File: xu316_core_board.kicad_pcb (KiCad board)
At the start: 2 copper layers, 60.5 x 67.8 mm, 91 parts, among them CN1 HX JN1.27-2x10P ZZ H4.9, J1 Conn_01x08, J10 Conn_02x04_Odd_Even, J11 Conn_02x05_Odd_Even, J12 Conn_02x04_Odd_Even, J13 Conn_02x05_Odd_Even, J2 Conn_01x06, J3 Conn_01x10, J4 Conn_01x08, J5 Conn_02x05_Odd_Even, J6 Conn_02x02_Odd_Even, J7 Conn_02x04_Odd_Even, J8 Conn_01x02, J9 Conn_02x05_Odd_Even, Q1 SI1024X, SW1 RESET, U1 XU316-1024-QF60A-C32, U2 W25Q64JWUUIQ, U3 TPS62A0569PDRLR, U4 TPS62402DRCR, U5 LMR51450, U7 NUP4114, Y2 24MHz

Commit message: start routing
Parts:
- removed J5: Conn_02x05_Odd_Even, Connector_PinHeader_2.54mm:PinHeader_2x05_P2.54mm_Vertical
- added D1: D_Schottky_Small, Diode_SMD:D_SMA, F.Cu at (187.1, 102.1)
- added D2: D_Schottky_Small, Diode_SMD:D_SMA, F.Cu at (187.1, 106.6)
- added F1: 5A, Fuse:Fuse_2512_6332Metric, F.Cu at (138.2, 60.5)
- added FB1: 120R 2A, Inductor_SMD:L_0603_1608Metric, F.Cu at (178.7, 117.8)
- added J15: Jack-DC, Connector_BarrelJack:BarrelJack_CUI_PJ-063AH_Horizontal, F.Cu at (138.1, 54.6)
- added J16: Conn_02x06_Odd_Even, Connector_PinHeader_2.54mm:PinHeader_2x06_P2.54mm_Vertical, F.Cu at (107.0, 80.2)
- added R22: 0.1, Resistor_SMD:R_0402_1005Metric, F.Cu at (184.5, 109.9)
- added R23: 0.1, Resistor_SMD:R_0402_1005Metric, F.Cu at (184.5, 111.9)
- L1: footprint Inductor_SMD:L_0402_1005Metric -> Inductor_SMD:L_1008_2520Metric
- moved C21 92.2 mm to (130.0, 78.0)
- moved U3 90.3 mm to (129.5, 79.6), turned to -90 degrees
- moved C23 82.7 mm to (133.5, 81.7), turned to -90 degrees
- moved L1 82.1 mm to (132.6, 78.8), turned to -90 degrees
- moved R6 81.6 mm to (133.5, 83.6), turned to -90 degrees
- moved R5 80.8 mm to (132.5, 81.7), turned to 90 degrees
- moved Y2 79.2 mm to (120.9, 90.5)
- moved C22 79.1 mm to (130.4, 81.8), turned to 90 degrees
- moved R4 78.7 mm to (131.4, 81.7), turned to -90 degrees
- moved C3 76.9 mm to (122.9, 90.2), turned to -90 degrees
- moved C2 72.2 mm to (118.9, 90.8), turned to -90 degrees
- moved J11 68.6 mm to (109.9, 59.4), turned to 90 degrees
- moved R3 64.8 mm to (120.5, 88.7), turned to 180 degrees
- moved R2 62.1 mm to (118.9, 88.9), turned to -90 degrees
- moved L3 61.9 mm to (133.4, 91.2)
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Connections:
- C21 pad 1: +5V -> +5V(CORE)
- C24 pad 1: +5V -> +5V(IO)
- R7 pad 1: +5V -> +5V(IO)
- R8 pad 1: +5V -> +5V(IO)
- U2 pad 2: /X0P16A2 -> /X0P16A3
- U3 pad 3: +5V -> +5V(CORE)
- U3 pad 5: +5V -> +5V(CORE)
- U4 pad 3: +5V -> +5V(IO)
- U4 pad 5: +5V -> +5V(IO)
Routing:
- net +0.9V: track 0.00 -> 16.6 mm, vias 0 -> 4
- net /X0P1B0: track 0.00 -> 8.60 mm
- net /X0P16A3: track 0.00 -> 7.11 mm
- net /X0P16A4: track 0.00 -> 5.80 mm
- net /XU316 Core/XOUT: track 0.00 -> 3.78 mm
- net /X0P16A2: track 0.00 -> 3.31 mm
- net /XU316 Core/XIN: track 0.00 -> 2.58 mm
- net Net-(C2-Pad1): track 0.00 -> 2.57 mm
- net GND: vias 0 -> 16
- added copper zone on B.Cu, net GND
- added copper zone on F.Cu, net GND
- added copper zone on In1.Cu, net GND
- added copper zone on In2.Cu, net GND
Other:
- board size 60.5 x 67.8 mm -> 53.3 x 68.6 mm
- copper layers 2 -> 4

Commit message: sync
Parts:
- moved CN1 12.3 mm to (124.5, 99.0)
- moved C12 12.0 mm to (130.9, 88.5), turned to 0 degrees
- moved R10 11.0 mm to (136.8, 90.7)
- moved C26 7.75 mm to (133.5, 86.5), turned to 180 degrees
- moved C1 7.35 mm to (118.0, 83.7), turned to -90 degrees
- moved C22 4.76 mm to (127.9, 77.7), turned to -90 degrees
- moved C25 4.05 mm to (131.4, 94.2), turned to 90 degrees
- moved R7 3.70 mm to (129.9, 94.7), turned to 0 degrees
- moved L2 3.62 mm to (133.3, 93.2), turned to -90 degrees
- moved R6 3.60 mm to (130.4, 81.7)
- moved U3 3.05 mm to (132.6, 79.6), turned to 90 degrees
- moved R9 2.94 mm to (137.9, 90.7)
- moved C21 2.87 mm to (132.8, 78.0), turned to 180 degrees
- moved L1 2.76 mm to (129.8, 78.7), turned to 90 degrees
- moved R8 2.71 mm to (129.9, 93.6), turned to 0 degrees
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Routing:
- net +0.9V: track 16.6 -> 25.8 mm, vias 4 -> 6
- net /X0P16A5: track 0.00 -> 9.09 mm
- net /X0P1C0: track 0.00 -> 9.06 mm
- net Net-(U4-EN2): track 0.00 -> 7.45 mm, vias 0 -> 2
- net +1.8V: track 0.00 -> 7.40 mm, vias 0 -> 2
- net +3.3V: track 0.00 -> 7.37 mm, vias 0 -> 2
- net Net-(U4-EN1): track 0.00 -> 6.51 mm, vias 0 -> 2
- net /X0P16A2: track 3.31 -> 9.05 mm
- net Net-(U3-FB): track 0.00 -> 5.08 mm
- net /X0P16A4: track 5.80 -> 9.02 mm
- net /X0P16A3: track 7.11 -> 8.99 mm
- net +5V(CORE): track 0.00 -> 1.69 mm
- net +5V(IO): track 0.00 -> 1.67 mm
- added copper zone on In2.Cu, net +0.9V
- added copper zone on F.Cu, net +5V(CORE)
- added copper zone on F.Cu, net +5V(IO)
- added copper zone on F.Cu, net Net-(U3-SW)
- added copper zone on F.Cu, net Net-(U4-SW1)
- added copper zone on F.Cu, net Net-(U4-SW2)

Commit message: Routed the power rail
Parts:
- moved R10 6.81 mm to (133.1, 85.0)
- moved R9 6.79 mm to (134.2, 85.0)
- moved C12 5.97 mm to (125.1, 90.1), turned to -90 degrees
- moved C26 0.61 mm to (132.9, 86.5)
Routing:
- net +5V(IO): track 1.67 -> 4.60 mm
- net +0.9V: track 25.8 -> 28.5 mm, vias 6 -> 7
- net +1.8V: track 7.40 -> 9.83 mm, vias 2 -> 6
- net GND: track 0.00 -> 0.43 mm, vias 16 -> 17
- net +3.3V: track 7.37 -> 7.33 mm, vias 2 -> 3
- added copper zone on F.Cu, net +1.8V
- added copper zone on In2.Cu, net +1.8V
- added copper zone on F.Cu, net +3.3V
- added copper zone on In2.Cu, net +3.3V

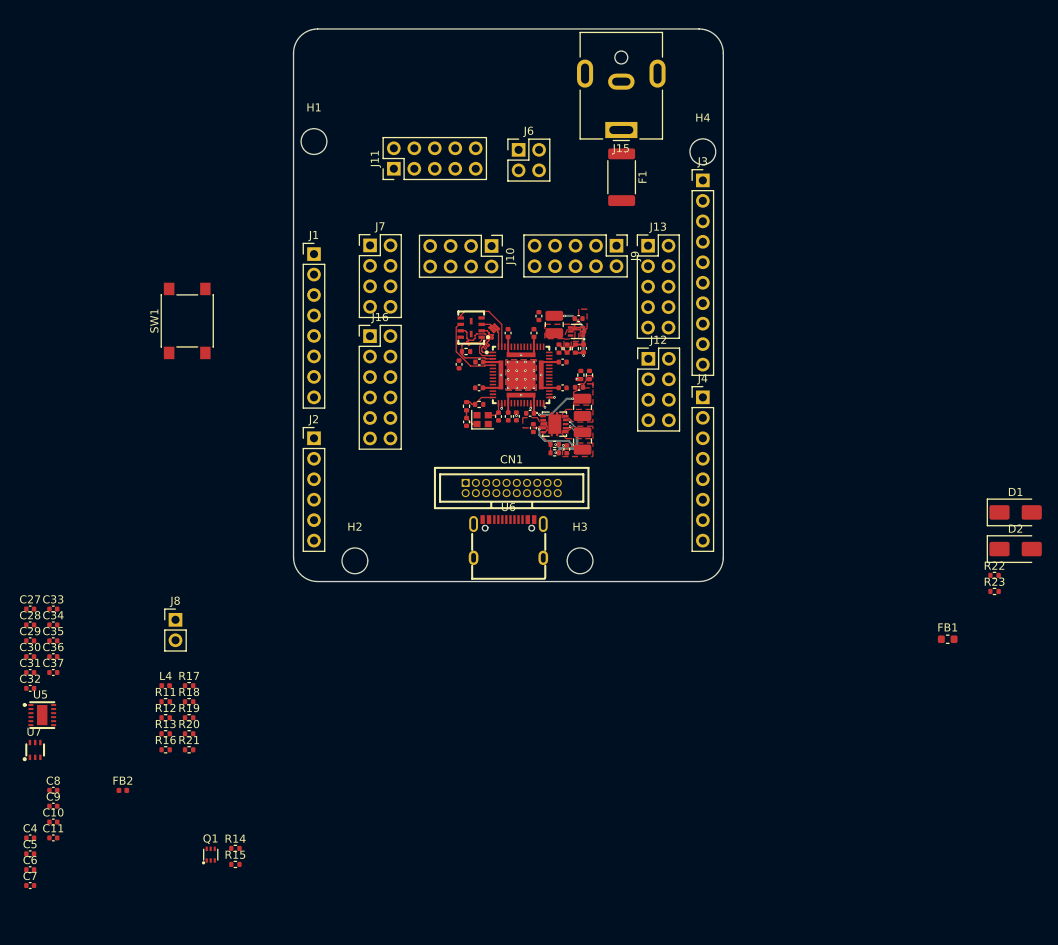
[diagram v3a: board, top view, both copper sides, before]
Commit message: Updated schem; Routed most of the IO
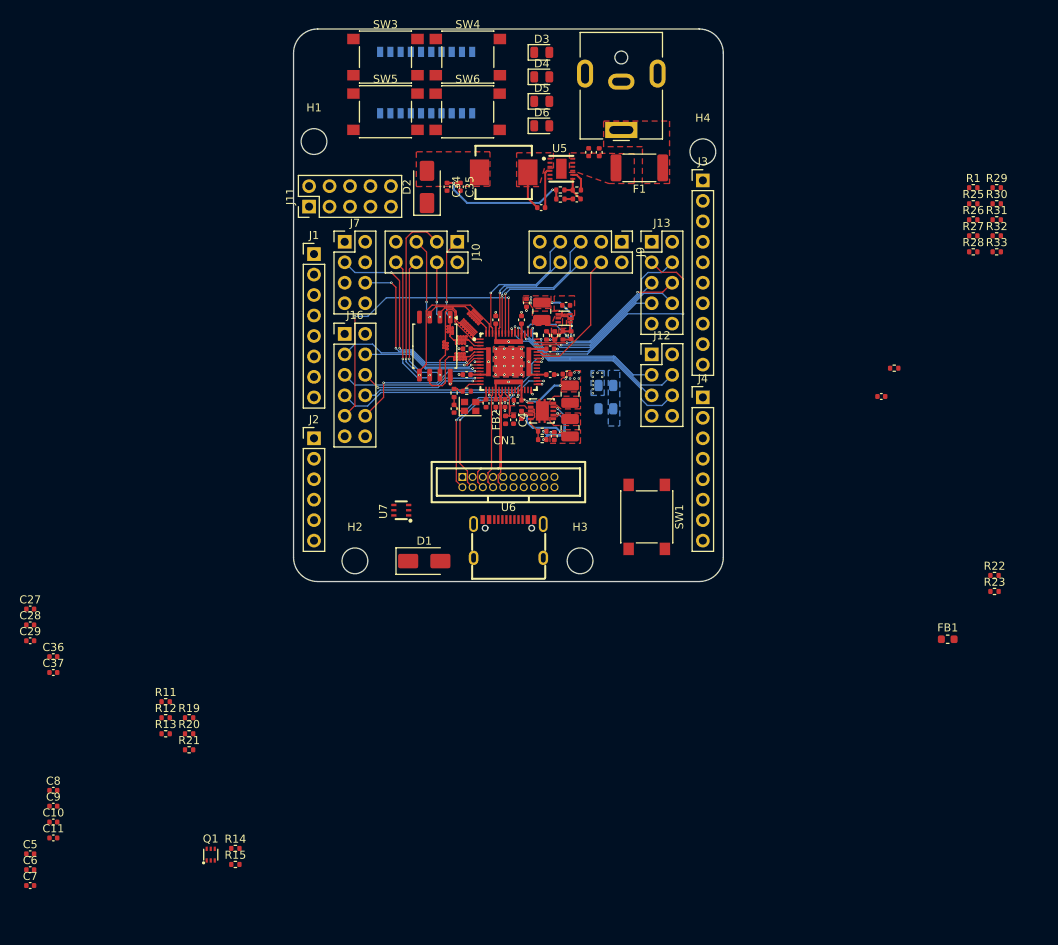
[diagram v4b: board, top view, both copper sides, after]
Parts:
- removed C1: 100N, Capacitor_SMD:C_0402_1005Metric
- removed J6: Conn_02x02_Odd_Even, Connector_PinHeader_2.54mm:PinHeader_2x02_P2.54mm_Vertical
- removed J8: Conn_01x02, Connector_PinHeader_2.54mm:PinHeader_1x02_P2.54mm_Vertical
- removed L4: 4.7uH, Inductor_SMD:L_0402_1005Metric
- removed U2: W25Q64JWUUIQ, EasyEDA_Lib:USON-8_L4.0-W3.0-P0.80-BL_WINBOND_UU
- added C38: 100N, Capacitor_SMD:C_0402_1005Metric, F.Cu at (170.4, 87.7)
- added D3: LED_GRN, LED_SMD:LED_0805_2012Metric, F.Cu at (128.3, 45.0)
- added D4: LED_GRN, LED_SMD:LED_0805_2012Metric, F.Cu at (128.3, 48.0)
- added D5: LED_GRN, LED_SMD:LED_0805_2012Metric, F.Cu at (128.3, 51.0)
- added D6: LED_GRN, LED_SMD:LED_0805_2012Metric, F.Cu at (128.3, 54.1)
- added L5: 4.7uH, EasyEDA_Lib:IND-SMD_L7.0-W6.6, F.Cu at (123.5, 59.9)
- added R24: 4.7K, Resistor_SMD:R_0402_1005Metric, F.Cu at (172.0, 84.2)
- added R25: 4.7K, Resistor_SMD:R_0402_1005Metric, F.Cu at (181.8, 63.8)
- added R26: 470, Resistor_SMD:R_0402_1005Metric, F.Cu at (181.8, 65.7)
- added R27: 470, Resistor_SMD:R_0402_1005Metric, F.Cu at (181.8, 67.7)
- added R28: 470, Resistor_SMD:R_0402_1005Metric, F.Cu at (181.8, 69.7)
- added R29: 470, Resistor_SMD:R_0402_1005Metric, F.Cu at (184.7, 61.8)
- added R30: 10K, Resistor_SMD:R_0402_1005Metric, F.Cu at (184.7, 63.8)
- added R31: 10K, Resistor_SMD:R_0402_1005Metric, F.Cu at (184.7, 65.7)
- added R32: 10K, Resistor_SMD:R_0402_1005Metric, F.Cu at (184.7, 67.7)
- added R33: 10K, Resistor_SMD:R_0402_1005Metric, F.Cu at (184.7, 69.7)
- added SW3: SW_Push, Button_Switch_SMD:SW_Push_1P1T_NO_6x6mm_H9.5mm, F.Cu at (108.9, 45.5)
- added SW4: SW_Push, Button_Switch_SMD:SW_Push_1P1T_NO_6x6mm_H9.5mm, F.Cu at (119.1, 45.5)
- added SW5: SW_Push, Button_Switch_SMD:SW_Push_1P1T_NO_6x6mm_H9.5mm, F.Cu at (108.9, 52.3)
- added SW6: SW_Push, Button_Switch_SMD:SW_Push_1P1T_NO_6x6mm_H9.5mm, F.Cu at (119.1, 52.3)
- added SW7: ~, EasyEDA_Lib:SW-SMD_20P-L14.3-W5.4-P1.27-LS8.3, B.Cu at (113.9, 48.7)
- added U8: W25Q32JVSS, Package_SO:SOIC-8_5.23x5.23mm_P1.27mm, F.Cu at (115.0, 81.4)
- C2, C3: value 100N -> 22pF
- C4: value 100N -> 1uF
- R10, R9: footprint Resistor_SMD:R_0402_1005Metric -> Resistor_SMD:R_0805_2012Metric; moved to B.Cu
- moved C31 95.7 mm to (135.4, 57.4), turned to 90 degrees
- moved U5 93.5 mm to (130.7, 59.4)
- moved C30 93.4 mm to (134.1, 57.4), turned to 90 degrees
- moved C32 87.1 mm to (128.2, 64.2), turned to 180 degrees
- moved R16 86.2 mm to (132.6, 62.0)
- moved D2 85.8 mm to (114.0, 61.7), turned to 90 degrees
- moved C33 82.5 mm to (132.6, 63.2)
- moved C4 79.3 mm to (124.8, 90.6), turned to -90 degrees
- moved R18 77.6 mm to (130.6, 63.2)
- moved R17 76.9 mm to (130.6, 62.0)
- moved C35 75.7 mm to (118.2, 61.6), turned to -90 degrees
- moved D1 73.6 mm to (113.7, 108.1)
- moved C34 73.1 mm to (116.5, 61.6), turned to -90 degrees
- moved R1 66.1 mm to (181.8, 61.8), turned to 0 degrees
- moved FB2 66.1 mm to (123.8, 90.6), turned to 90 degrees
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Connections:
- CN1 pad 13: Net-(CN1-Pad13) -> GND
- CN1 pad 15: Net-(CN1-Pad13) -> GND
- CN1 pad 17: Net-(CN1-Pad13) -> GND
- CN1 pad 19: Net-(CN1-Pad13) -> GND
- CN1 pad 3: Net-(CN1-Pad13) -> GND
- CN1 pad 5: Net-(CN1-Pad13) -> GND
- CN1 pad 7: Net-(CN1-Pad13) -> GND
- CN1 pad 9: Net-(CN1-Pad13) -> GND
- J13 pad 4: VDDIO -> /X0P16B9
- J13 pad 6: /X0P16B9 -> /X0P16B11
- J13 pad 8: /X0P16B11 -> /CORE_ADJ
- J3 pad 10: /X0P16B14 -> /X0P16B5
- J3 pad 5: /X0P16B9 -> /X0P1C0
- J3 pad 8: /X0P1D0 -> /X0P16B9
- J3 pad 9: /X0P16B5 -> /X0P16B14
- J4 pad 7: /X0P1C0 -> /X0P1D0
- J9 pad 3: /X0P16B3 -> VDDIO
- J9 pad 4: VDDIO -> /X0P16B3
- J9 pad 5: /X0P16B4 -> /X0P16B5
- J9 pad 6: /X0P16B5 -> /X0P16B4
- J9 pad 7: /X0P16B6 -> /X0P16B7
- J9 pad 8: /X0P16B7 -> /X0P16B6
- Q1 pad 1: /X0P16B11 -> /IO Headers/SDA_XMOS
- Q1 pad 2: VDDIO_I2C -> VDDIO
- Q1 pad 3: /IO Headers/I2C_SCL_PU -> /IO Headers/SCL_ARD
- Q1 pad 4: /X0P16B10 -> /IO Headers/SCL_XMOS
- Q1 pad 5: VDDIO_I2C -> VDDIO
- Q1 pad 6: /IO Headers/I2C_SDA_PU -> /IO Headers/SDA_ARD
- R1 pad 2: /X0P1B0 -> /IO Headers/SCL_XMOS
- R14 pad 2: /IO Headers/I2C_SCL_PU -> /IO Headers/SCL_ARD
- R15 pad 2: /IO Headers/I2C_SDA_PU -> /IO Headers/SDA_ARD
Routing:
- net /X1P1K0: track 0.00 -> 37.3 mm, vias 0 -> 2
- net /X0P16A2: track 9.05 -> 40.9 mm, vias 0 -> 2
- net /X0P1L0: track 0.00 -> 29.4 mm, vias 0 -> 2
- net /X1P1F0: track 0.00 -> 27.4 mm, vias 0 -> 1
- net /X0P1A0: track 0.00 -> 27.3 mm, vias 0 -> 3
- net /X0P16A5: track 9.09 -> 35.6 mm, vias 0 -> 2
- net /X0P1C0: track 9.06 -> 35.6 mm, vias 0 -> 2
- net /X0P16B15: track 0.00 -> 26.3 mm, vias 0 -> 1
- net /X1P1G0: track 0.00 -> 25.4 mm, vias 0 -> 1
- net /X0P1D0: track 0.00 -> 23.3 mm, vias 0 -> 3
- net /X0P16B13: track 0.00 -> 23.2 mm, vias 0 -> 1
- net /X0P16B11: track 0.00 -> 22.9 mm, vias 0 -> 2
- net /X0P16B9: track 0.00 -> 21.9 mm, vias 0 -> 1
- net /X0P1B0: track 9.07 -> 28.7 mm, vias 0 -> 2
- net /X0P16A4: track 9.02 -> 28.6 mm, vias 0 -> 2
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- added copper zone on F.Cu, net +0.9V
- added copper zone on B.Cu, net +3.3V
- added copper zone on F.Cu, net +Vin
- added copper zone on F.Cu, net DCDC_5V
- added copper zone on F.Cu, net Net-(C32-Pad2)
- added copper zone on F.Cu, net Net-(F1-Pad1)
- added copper zone on B.Cu, net VDDIO
- added copper zone on In2.Cu, net VDDIO

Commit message: Finish routing
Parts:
- removed R23: 0.1, Resistor_SMD:R_0402_1005Metric
- added J14: Conn_01x02, Connector_PinHeader_2.54mm:PinHeader_1x02_P2.54mm_Vertical, F.Cu at (103.9, 99.1)
- added J17: Conn_01x03, Connector_PinHeader_2.54mm:PinHeader_1x03_P2.54mm_Vertical, F.Cu at (136.4, 96.8)
- added J5: Conn_01x03, Connector_PinHeader_2.54mm:PinHeader_1x03_P2.54mm_Vertical, F.Cu at (148.3, 46.9)
- added J6: Conn_01x04, Connector_PinHeader_2.54mm:PinHeader_1x04_P2.54mm_Vertical, F.Cu at (99.4, 61.6)
- added J8: Conn_01x02, Connector_PinHeader_2.54mm:PinHeader_1x02_P2.54mm_Vertical, F.Cu at (124.2, 68.5)
- added R34: 0.1, Resistor_SMD:R_1206_3216Metric, F.Cu at (121.0, 69.7)
- J11: value Conn_02x05_Odd_Even -> Conn_01x03; footprint Connector_PinHeader_2.54mm:PinHeader_2x05_P2.54mm_Vertical -> Connector_PinHeader_2.54mm:PinHeader_1x03_P2.54mm_Vertical
- R22: footprint Resistor_SMD:R_0402_1005Metric -> Resistor_SMD:R_1206_3216Metric
- moved R15 97.0 mm to (143.5, 64.6), turned to 90 degrees
- moved R14 97.0 mm to (143.5, 62.7), turned to -90 degrees
- moved Q1 96.6 mm to (140.4, 63.9), turned to 180 degrees
- moved C6 90.9 mm to (124.7, 78.1), turned to 90 degrees
- moved C5 89.3 mm to (129.4, 82.8)
- moved C11 87.3 mm to (132.3, 83.7)
- moved R30 84.5 mm to (102.8, 43.3)
- moved C7 84.2 mm to (118.9, 83.8), turned to 180 degrees
- moved R32 83.8 mm to (102.8, 50.1)
- moved C10 81.6 mm to (129.3, 87.1)
- moved C9 81.0 mm to (129.3, 86.1)
- moved R22 79.7 mm to (105.2, 102.3)
- moved C27 73.7 mm to (137.6, 102.6), turned to -90 degrees
- moved C8 70.8 mm to (121.4, 90.5), turned to -90 degrees
- moved R13 69.7 mm to (132.3, 81.6), turned to 180 degrees
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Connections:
- J11 pad 1: +5V -> +1.8V
- J11 pad 2: +3.3V -> +1.8V
- J11 pad 3: +5V -> GND
- J3 pad 1: /IO Headers/I2C_SCL_PU -> /IO Headers/SCL_ARD
- J3 pad 2: /IO Headers/I2C_SDA_PU -> /IO Headers/SDA_ARD
- J7 pad 4: VDDIO -> /X0P1D0
- J7 pad 5: /X0P1C0 -> GND
- J7 pad 6: /X0P1D0 -> GND
- R22 pad 1: +5V(IO) -> +5V
- R22 pad 2: +5V -> +5V(IO)
- R27 pad 1: /IO Headers/LED0 -> /IO Headers/LED1
- R28 pad 1: /IO Headers/LED0 -> /IO Headers/LED2
- R29 pad 1: /IO Headers/LED0 -> /IO Headers/LED3
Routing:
- net +3.3V: track 7.33 -> 221.7 mm, vias 18 -> 16
- net +1.8V: track 9.38 -> 154.2 mm, vias 5 -> 13
- net /RST_N: track 12.5 -> 115.1 mm, vias 0 -> 1
- net VDDIO: track 18.4 -> 96.5 mm, vias 4 -> 25
- net /X1P1G0: track 25.4 -> 99.2 mm, vias 1 -> 2
- net /X1P1D0: track 15.3 -> 85.1 mm, vias 2 -> 4
- net /X0P1D0: track 23.3 -> 89.6 mm, vias 3 -> 7
- net /X0P1A0: track 27.3 -> 93.2 mm, vias 3 -> 7
- net +Vin: track 0.00 -> 64.9 mm, vias 0 -> 15
- net /X1P1C0: track 17.7 -> 79.5 mm, vias 1 -> 3
- net /X1P1K0: track 37.3 -> 95.1 mm, vias 2 -> 4
- net /X1P1B0: track 15.1 -> 72.3 mm, vias 1 -> 2
- net /X1P1F0: track 27.4 -> 82.3 mm, vias 1 -> 3
- net /X1P1A0: track 18.7 -> 70.3 mm, vias 1 -> 2
- net /X1P16A7: track 17.7 -> 67.2 mm, vias 2 -> 3
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- added copper zone on B.Cu, net +1.8V
- added copper zone on F.Cu, net +5V
- added copper zone on In2.Cu, net +5V
- added copper zone on In2.Cu, net +5V(CORE)
- added copper zone on In2.Cu, net +5V(IO)
- added copper zone on In2.Cu, net +Vin
- added copper zone on In2.Cu, net USB_5V
- added copper zone on In2.Cu, net VBUS
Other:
- board text added: "1V8"
- board text added: "3V3"
- board text added: "4"
- board text added: "5"
- board text added: "5V"
- board text added: "6"
- board text added: "7"
- board text added: "A"
- board text added: "A3"
- board text added: "B"
- board text added: "B0"
- board text added: "B1"
- board text added: "B2"
- board text added: "B3"
- board text added: "BTN0"
- board text added: "BTN1"
- board text added: "BTN2"
- board text added: "BTN3"
- board text added: "C"
- board text added: "D"
- board text added: "E2"
- board text added: "E3"
- board text added: "F"
- board text added: "F1"
- board text added: "F2"
- board text added: "F3"
- board text added: "Function Switch"
- board text added: "G"
- board text added: "I2C VDD"
- board text added: "K"
- board text added: "L"
- board text added: "LED0"
- board text added: "LED1"
- board text added: "LED2"
- board text added: "LED3"
- board text added: "M"
- board text added: "N"
- board text added: "O"
- board text added: "P"
- board text added: "RESET"
- board text added: "SCL"
- board text added: "SDA"
- board text added: "T0"
- board text added: "T0P8D"
- board text added: "T1"
- board text added: "VDDIO Switch R9: ⎓3V3 R10: ⎓1V8"
- board text added: "⎓"
- board text added: "⏚"
